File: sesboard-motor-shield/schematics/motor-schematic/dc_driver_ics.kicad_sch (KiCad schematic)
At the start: 10 parts, among them J2 EXTERNAL_MOTOR_POWER, U2 L293D, U3 L293D, U5 L293D

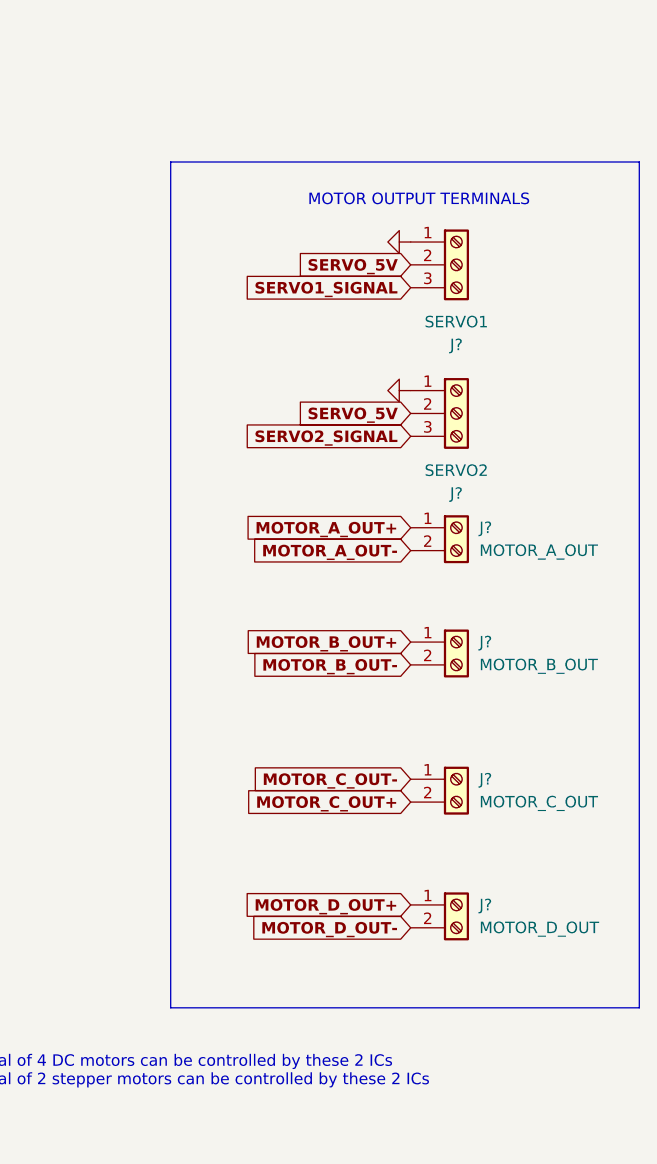
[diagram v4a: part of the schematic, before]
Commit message: added stepper connector
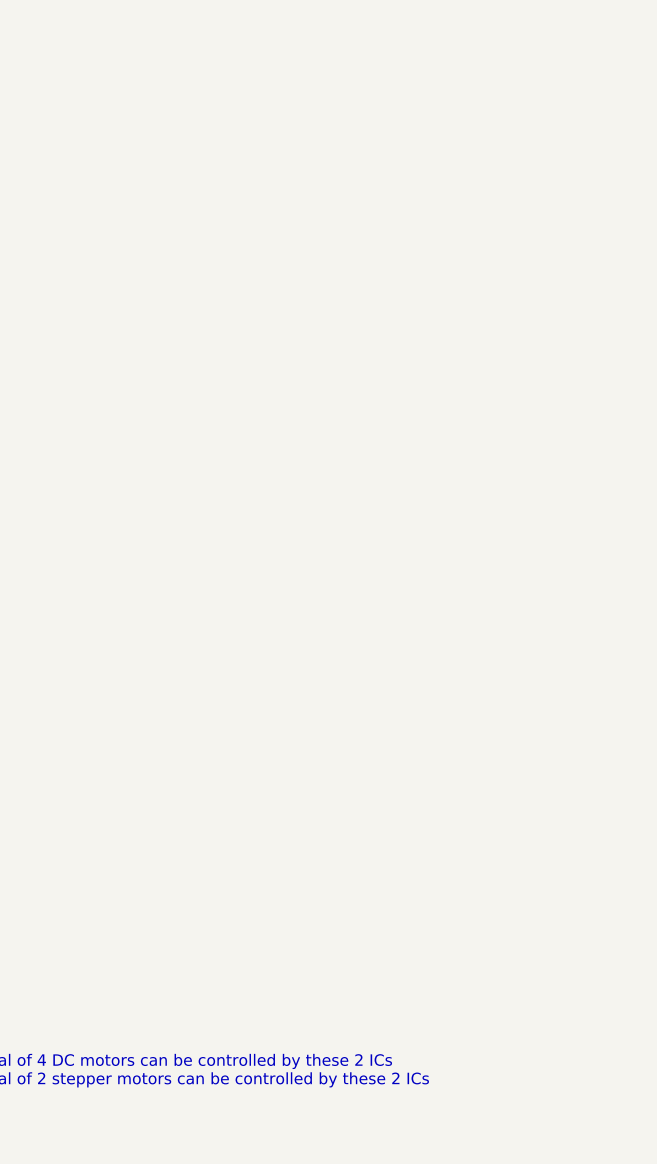
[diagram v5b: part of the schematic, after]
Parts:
- removed J?: MOTOR_C_OUT, TerminalBlock_Phoenix:TerminalBlock_Phoenix_MKDS-1,5-2_1x02_P5.00mm_Horizontal, symbol Connector:Screw_Terminal_01x02
- removed J?: MOTOR_D_OUT, TerminalBlock_Phoenix:TerminalBlock_Phoenix_MKDS-1,5-2_1x02_P5.00mm_Horizontal, symbol Connector:Screw_Terminal_01x02
- removed J?: MOTOR_A_OUT, TerminalBlock_Phoenix:TerminalBlock_Phoenix_MKDS-1,5-2_1x02_P5.00mm_Horizontal, symbol Connector:Screw_Terminal_01x02
- removed J?: SERVO1, Connector_PinHeader_2.54mm:PinHeader_1x03_P2.54mm_Vertical, symbol Connector:Screw_Terminal_01x03
- removed J?: MOTOR_B_OUT, TerminalBlock_Phoenix:TerminalBlock_Phoenix_MKDS-1,5-2_1x02_P5.00mm_Horizontal, symbol Connector:Screw_Terminal_01x02
- removed J?: SERVO2, Connector_PinHeader_2.54mm:PinHeader_1x03_P2.54mm_Vertical, symbol Connector:Screw_Terminal_01x03
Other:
- note removed: "MOTOR OUTPUT TERMINALS"

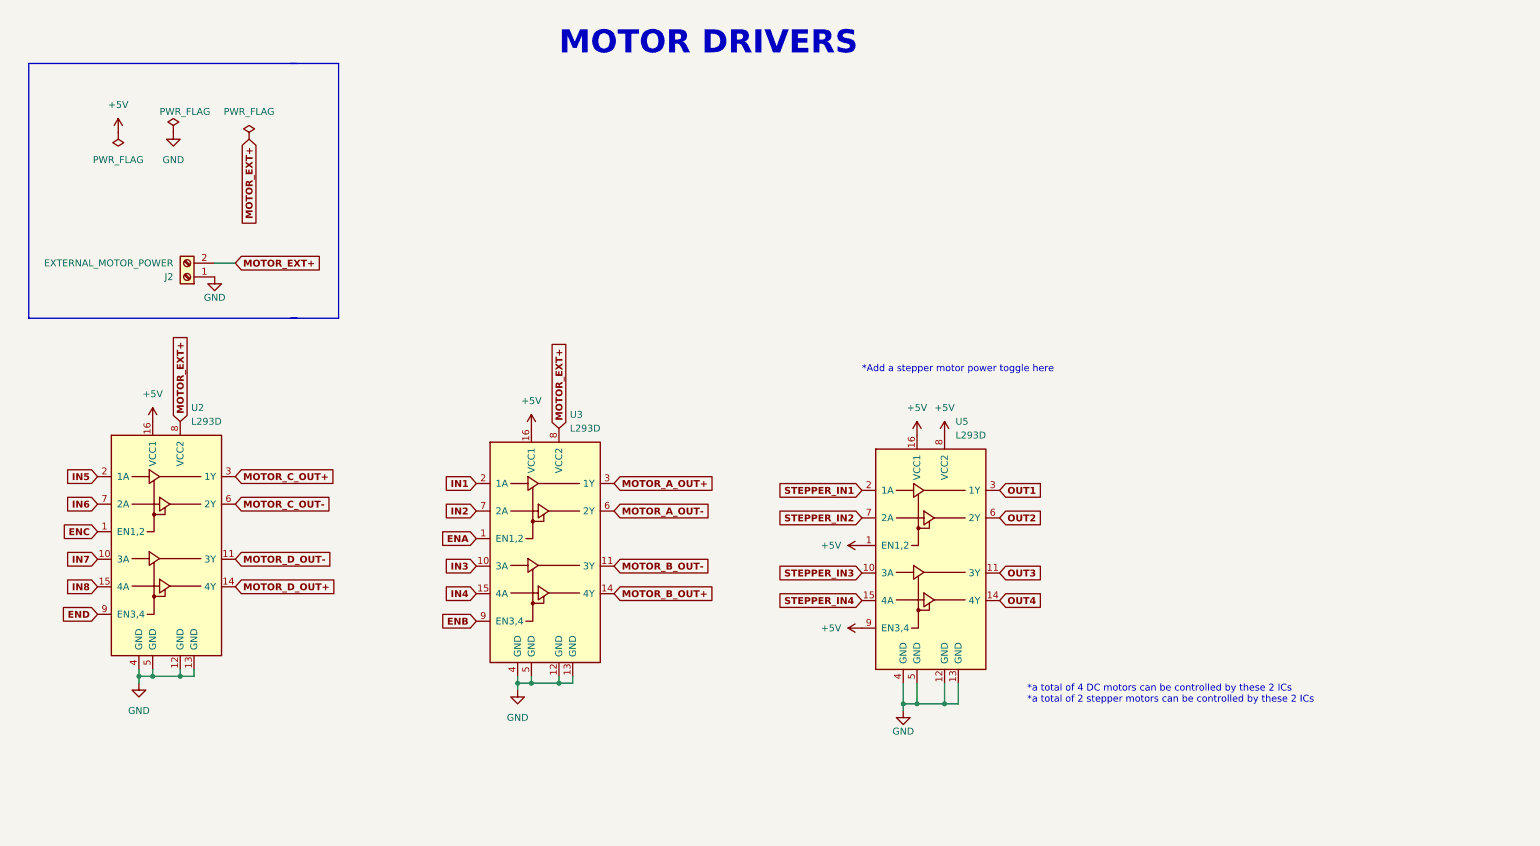
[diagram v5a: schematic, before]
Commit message: added power toggle
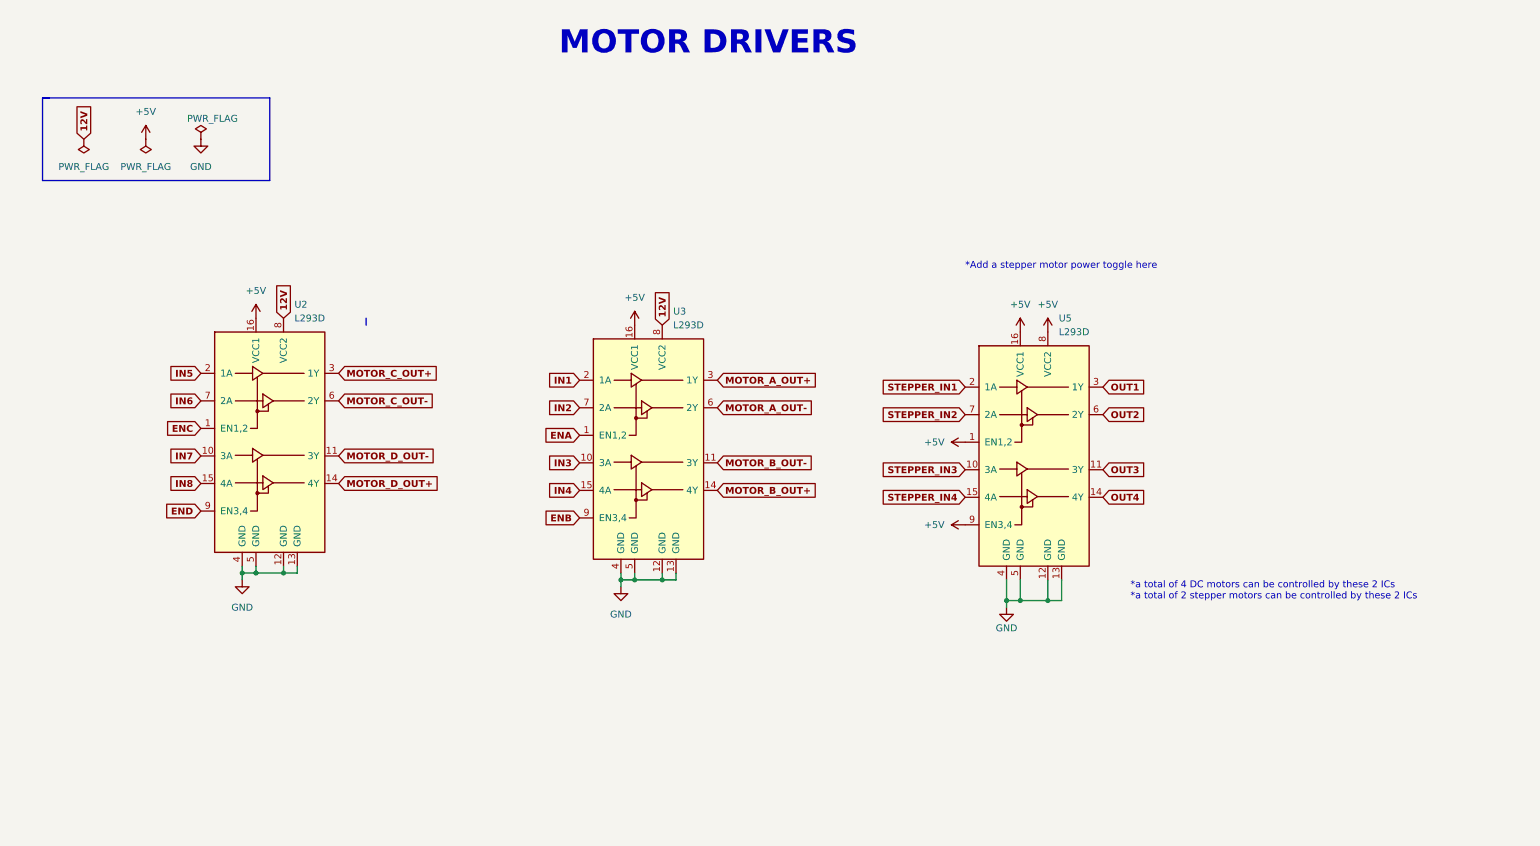
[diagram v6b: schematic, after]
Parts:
- removed J2: EXTERNAL_MOTOR_POWER, TerminalBlock_Phoenix:TerminalBlock_Phoenix_MKDS-1,5-2_1x02_P5.00mm_Horizontal, symbol Connector:Screw_Terminal_01x02
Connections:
- net MOTOR_EXT+ renamed 12V
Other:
- moved on the sheet: U2, U3, U5
